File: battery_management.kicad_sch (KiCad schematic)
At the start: 25 parts, among them J3 Conn_01x02, J7 Conn_01x02, Q1 CSD18534Q5A, Q2 CSD18534Q5A, Q3 Si7465DP, U1 BQ25896RTWT, U2 BQ29705DSET

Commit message: footprints
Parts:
- C_BAT1, C_IN1: footprint (none) -> Capacitor_SMD:C_0805_2012Metric
- C_BTST1: renamed from C_BTST; footprint (none) -> Capacitor_SMD:C_0402_1005Metric
- C_PMID1: renamed from C_PMID; footprint (none) -> Capacitor_SMD:C_0402_1005Metric
- C_PROT1: renamed from C_PROT; footprint (none) -> Capacitor_SMD:C_0402_1005Metric
- C_REGN1: renamed from C_REGN; footprint (none) -> Capacitor_SMD:C_0402_1005Metric
- C_SYS1: renamed from C_SYS; footprint (none) -> Capacitor_SMD:C_0805_2012Metric
- J3: footprint (none) -> Connector_Wire:SolderWire-2.5sqmm_1x02_P8.8mm_D2.4mm_OD4.4mm
- J7: footprint (none) -> Connector_Wire:SolderWire-0.5sqmm_1x02_P4.6mm_D0.9mm_OD2.1mm
- L1: footprint (none) -> Inductor_SMD:L_7.3x7.3_H3.5
- R1, R19, R2, R20, R5, R_G1, R_G2: footprint (none) -> Resistor_SMD:R_0402_1005Metric
- R_QON1: renamed from R_QON; footprint (none) -> Resistor_SMD:R_0402_1005Metric
- R_REV1: renamed from R_REV; footprint (none) -> Resistor_SMD:R_0402_1005Metric
- R_SENSE_FG1: renamed from R_SENSE_FG; footprint (none) -> Resistor_SMD:R_2512_6332Metric
- U1: footprint RTW0024H -> Package_DFN_QFN:Texas_RTW_WQFN-24-1EP_4x4mm_P0.5mm_EP2.7x2.7mm_ThermalVias
- U2: footprint DSE0006A -> BQ29705DSET:SON50P150X150X80-6N
- renumbered Q3 to Q_REV1
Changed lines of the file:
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@@
 		(dnp no)
 		(fields_autoplaced yes)
-		(property "Reference" "C_PROT"
+		(property "Reference" "C_PROT1"
 			(at 38.1 123.1899 0)
 			(effects
@@
 			)
 		)
-		(property "Footprint" ""
+		(property "Footprint" "Capacitor_SMD:C_0402_1005Metric"
 			(at 35.2552 128.27 0)
 			(effects
@@
 			(project ""
 				(path "/96bcf3cc-a3b8-4386-8709-07acaf7b6253/a4f15ca0-ce5b-4b53-a9db-308ad3d3fa71"
-					(reference "C_PROT")
+					(reference "C_PROT1")
 					(unit 1)
 				)
@@
 		(dnp no)
 		(fields_autoplaced yes)
-		(property "Reference" "C_SYS"
+		(property "Reference" "C_SYS1"
 			(at 95.25 49.5299 0)
 			(effects
@@
 			)
 		)
-		(property "Footprint" ""
+		(property "Footprint" "Capacitor_SMD:C_0805_2012Metric"
 			(at 92.4052 54.61 0)
 			(effects
@@
 			(project ""
 				(path "/96bcf3cc-a3b8-4386-8709-07acaf7b6253/a4f15ca0-ce5b-4b53-a9db-308ad3d3fa71"
-					(reference "C_SYS")
+					(reference "C_SYS1")
 					(unit 1)
 				)
@@
 		(dnp no)
 		(fields_autoplaced yes)
-		(property "Reference" "R_SENSE_FG"
+		(property "Reference" "R_SENSE_FG1"
 			(at 147.32 143.5099 0)
 			(effects
@@
 			)
 		)
-		(property "Footprint" ""
+		(property "Footprint" "Resistor_SMD:R_2512_6332Metric"
 			(at 143.002 144.78 90)
 			(effects
@@
 			(project ""
 				(path "/96bcf3cc-a3b8-4386-8709-07acaf7b6253/a4f15ca0-ce5b-4b53-a9db-308ad3d3fa71"
-					(reference "R_SENSE_FG")
+					(reference "R_SENSE_FG1")
 					(unit 1)
 				)
@@
 			)
 		)
-		(property "Footprint" ""
+		(property "Footprint" "Capacitor_SMD:C_0805_2012Metric"
 			(at 37.7952 38.1 0)
 			(effects
@@
 		(dnp no)
 		(fields_autoplaced yes)
-		(property "Reference" "R_REV"
+		(property "Reference" "R_REV1"
 			(at 101.6 116.8399 0)
 			(effects
@@
 			)
 		)
-		(property "Footprint" ""
+		(property "Footprint" "Resistor_SMD:R_0402_1005Metric"
 			(at 97.282 118.11 90)
 			(effects
@@
 			(project ""
 				(path "/96bcf3cc-a3b8-4386-8709-07acaf7b6253/a4f15ca0-ce5b-4b53-a9db-308ad3d3fa71"
-					(reference "R_REV")
+					(reference "R_REV1")
 					(unit 1)
 				)
@@
 		(dnp no)
 		(fields_autoplaced yes)
-		(property "Reference" "C_REGN"
+		(property "Reference" "C_REGN1"
 			(at 93.98 62.2299 0)
 			(effects
@@
 			)
 		)
-		(property "Footprint" ""
+		(property "Footprint" "Capacitor_SMD:C_0402_1005Metric"
 			(at 91.1352 67.31 0)
 			(effects
@@
 			(project ""
 				(path "/96bcf3cc-a3b8-4386-8709-07acaf7b6253/a4f15ca0-ce5b-4b53-a9db-308ad3d3fa71"
-					(reference "C_REGN")
+					(reference "C_REGN1")
 					(unit 1)
 				)
@@
 		(dnp no)
 		(fields_autoplaced yes)
-		(property "Reference" "R_QON"
+		(property "Reference" "R_QON1"
 			(at 101.6 80.0099 0)
 			(effects
@@
 			)
 		)
-		(property "Footprint" ""
+		(property "Footprint" "Resistor_SMD:R_0402_1005Metric"
 			(at 97.282 81.28 90)
 			(effects
@@
 			(project ""
 				(path "/96bcf3cc-a3b8-4386-8709-07acaf7b6253/a4f15ca0-ce5b-4b53-a9db-308ad3d3fa71"
-					(reference "R_QON")
+					(reference "R_QON1")
 					(unit 1)
 				)
@@
 			)
 		)
-		(property "Footprint" ""
+		(property "Footprint" "Resistor_SMD:R_0402_1005Metric"
 			(at 87.122 86.36 90)
 			(effects
@@
 			)
 		)
-		(property "Footprint" ""
+		(property "Footprint" "Resistor_SMD:R_0402_1005Metric"
 			(at 61.722 114.3 90)
 			(effects
@@
 			)
 		)
-		(property "Footprint" ""
+		(property "Footprint" "Inductor_SMD:L_7.3x7.3_H3.5"
 			(at 104.14 45.72 0)
 			(effects
@@
 		(dnp no)
 		(fields_autoplaced yes)
-		(property "Reference" "C_PMID"
+		(property "Reference" "C_PMID1"
 			(at 41.91 44.4499 0)
 			(effects
@@
 			)
 		)
-		(property "Footprint" ""
+		(property "Footprint" "Capacitor_SMD:C_0402_1005Metric"
 			(at 39.0652 49.53 0)
 			(effects
@@
 			(project ""
 				(path "/96bcf3cc-a3b8-4386-8709-07acaf7b6253/a4f15ca0-ce5b-4b53-a9db-308ad3d3fa71"
-					(reference "C_PMID")
+					(reference "C_PMID1")
 					(unit 1)
 				)
@@
 			)
 		)
-		(property "Footprint" ""
+		(property "Footprint" "Resistor_SMD:R_0402_1005Metric"
 			(at 101.092 93.98 90)
 			(effects
@@
 			)
 		)
-		(property "Footprint" ""
+		(property "Footprint" "Resistor_SMD:R_0402_1005Metric"
 			(at 82.042 148.59 90)
 			(effects
@@
 		(dnp no)
 		(fields_autoplaced yes)
-		(property "Reference" "C_BTST"
+		(property "Reference" "C_BTST1"
 			(at 93.98 36.8299 0)
 			(effects
@@
 			)
 		)
-		(property "Footprint" ""
+		(property "Footprint" "Capacitor_SMD:C_0402_1005Metric"
 			(at 91.1352 41.91 0)
 			(effects
@@
 			(project ""
 				(path "/96bcf3cc-a3b8-4386-8709-07acaf7b6253/a4f15ca0-ce5b-4b53-a9db-308ad3d3fa71"
-					(reference "C_BTST")
+					(reference "C_BTST1")
 					(unit 1)
 				)
@@
 			)
 		)
-		(property "Footprint" "DSE0006A"
+		(property "Footprint" "BQ29705DSET:SON50P150X150X80-6N"
 			(at 63.5 139.7 0)
 			(effects
@@
 			)
 		)
-		(property "Footprint" "RTW0024H"
+		(property "Footprint" "Package_DFN_QFN:Texas_RTW_WQFN-24-1EP_4x4mm_P0.5mm_EP2.7x2.7mm_ThermalVias"
 			(at 63.5 68.58 0)
 			(effects
@@
 			)
 		)
-		(property "Footprint" ""
+		(property "Footprint" "Connector_Wire:SolderWire-0.5sqmm_1x02_P4.6mm_D0.9mm_OD2.1mm"
 			(at 128.27 90.17 0)
 			(effects
@@
 			)
 		)
-		(property "Footprint" ""
+		(property "Footprint" "Resistor_SMD:R_0402_1005Metric"
 			(at 84.582 135.89 90)
 			(effects
@@
 			)
 		)
-		(property "Footprint" ""
+		(property "Footprint" "Resistor_SMD:R_0402_1005Metric"
 			(at 31.242 53.34 90)
 			(effects
@@
 			)
 		)
-		(property "Footprint" ""
+		(property "Footprint" "Capacitor_SMD:C_0805_2012Metric"
 			(at 103.8352 73.66 0)
 			(effects
@@
 			)
 		)
-		(property "Footprint" ""
+		(property "Footprint" "Connector_Wire:SolderWire-2.5sqmm_1x02_P8.8mm_D2.4mm_OD4.4mm"
 			(at 161.29 119.38 0)
 			(effects
@@
 			)
 		)
-		(property "Footprint" ""
+		(property "Footprint" "Resistor_SMD:R_0402_1005Metric"
 			(at 94.742 147.32 90)
 			(effects
@@
 		(dnp no)
 		(fields_autoplaced yes)
-		(property "Reference" "Q3"
+		(property "Reference" "Q_REV1"
 			(at 118.11 113.0299 0)
 			(effects
@@
 			(project ""
 				(path "/96bcf3cc-a3b8-4386-8709-07acaf7b6253/a4f15ca0-ce5b-4b53-a9db-308ad3d3fa71"
-					(reference "Q3")
-					(unit 1)
-				)
+					(reference "Q_REV1")
+					(unit 1)
+				)

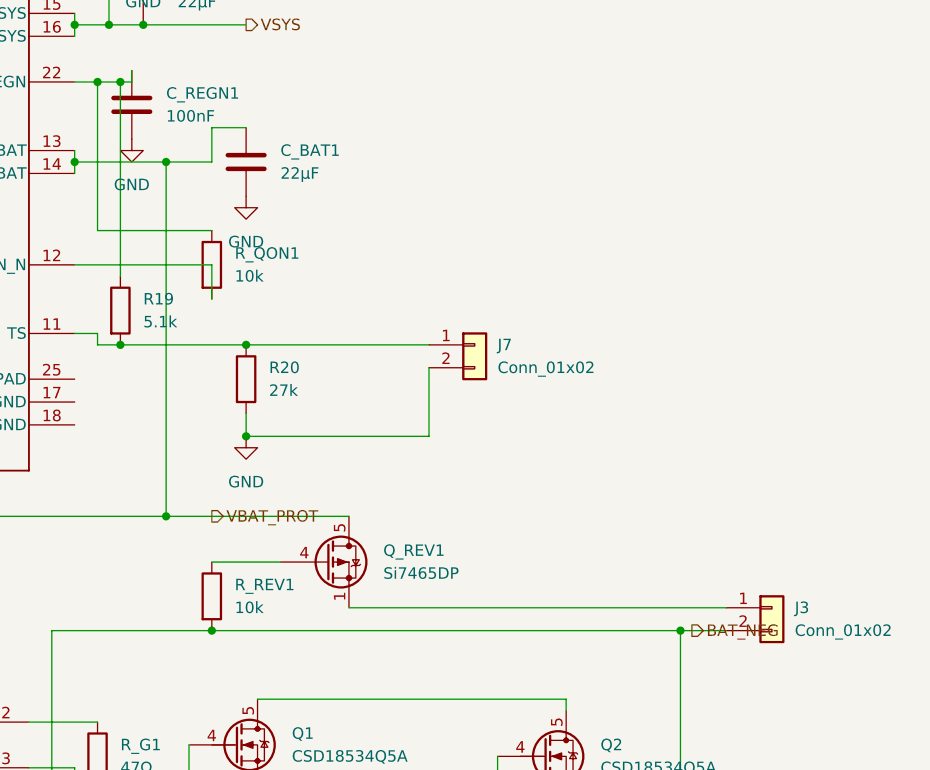
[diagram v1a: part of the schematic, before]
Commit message: fix missing connections, complete footprints
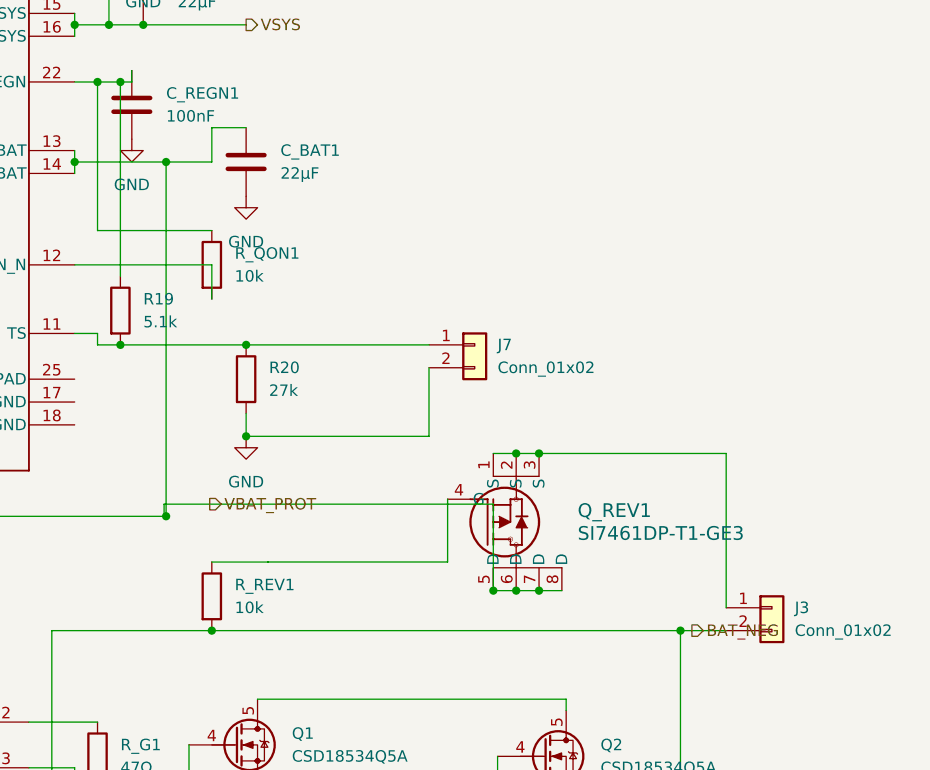
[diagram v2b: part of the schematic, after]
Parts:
- removed Q_REV1: Si7465DP, Package_SO:PowerPAK_SO-8_Single, symbol Si7461DP:Si7465DP
- added Q_REV1: SI7461DP-T1-GE3, Package_SO:PowerPAK_SO-8_Single, symbol Si7461DP-T1-GE3:SI7461DP-T1-GE3
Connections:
- net VBAT_PROT: now also Q_REV1.5 (D), Q_REV1.6 (D), Q_REV1.7 (D), Q_REV1.8 (D)
- net at R_REV1.1: now also Q_REV1.4 (G)
- net at J3.1 (Pin_1): now also Q_REV1.1 (S), Q_REV1.2 (S), Q_REV1.3 (S)
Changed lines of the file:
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@@
 	)
 	(junction
+		(at 130.3354 117.4769)
+		(diameter 0)
+		(color 0 0 0 0)
+	)
+	(junction
 		(at 83.82 54.61)
 		(diameter 0)
@@
 	)
 	(junction
+		(at 132.8754 102.2369)
+		(diameter 0)
+		(color 0 0 0 0)
+	)
+	(junction
 		(at 151.13 121.92)
 		(diameter 0)
@@
 	)
 	(junction
-		(at 99.06 121.92)
+		(at 135.4154 102.2369)
 		(diameter 0)
 		(color 0 0 0 0)
 	)
 	(junction
-		(at 91.44 54.61)
+		(at 132.8754 117.4769)
 		(diameter 0)
 		(color 0 0 0 0)
 	)
 	(junction
-		(at 88.9 60.96)
+		(at 93.98 109.2118)
 		(diameter 0)
 		(color 0 0 0 0)
 	)
 	(junction
-		(at 93.98 109.22)
+		(at 135.4154 117.4769)
+		(diameter 0)
+		(color 0 0 0 0)
+	)
+	(junction
+		(at 99.06 121.92)
+		(diameter 0)
+		(color 0 0 0 0)
+	)
+	(junction
+		(at 91.44 54.61)
+		(diameter 0)
+		(color 0 0 0 0)
+	)
+	(junction
+		(at 88.9 60.96)
 		(diameter 0)
 		(color 0 0 0 0)
@@
 	(wire
 		(pts
-			(xy 156.21 119.38) (xy 114.3 119.38)
+			(xy 93.7521 107.8693) (xy 93.7521 109.2118)
+		)
+		(stroke
+			(width 0)
+			(type default)
+		)
+	)
+	(wire
+		(pts
+			(xy 132.8754 102.2369) (xy 135.4154 102.2369)
 		)
 		(stroke
@@
 	(wire
 		(pts
-			(xy 99.06 114.3) (xy 106.68 114.3)
+			(xy 105.2984 114.2918) (xy 125.2554 114.2918)
 		)
 		(stroke
@@
 	(wire
 		(pts
+			(xy 130.3354 107.8693) (xy 130.3354 117.4769)
+		)
+		(stroke
+			(width 0)
+			(type default)
+		)
+	)
+	(wire
+		(pts
 			(xy 96.52 151.13) (xy 104.14 151.13)
 		)
@@
 	(wire
 		(pts
+			(xy 93.98 109.2118) (xy 93.98 109.22)
+		)
+		(stroke
+			(width 0)
+			(type default)
+		)
+	)
+	(wire
+		(pts
 			(xy 78.74 132.08) (xy 86.36 132.08)
 		)
@@
 	(wire
 		(pts
+			(xy 105.2984 114.2918) (xy 105.2984 114.3)
+		)
+		(stroke
+			(width 0)
+			(type default)
+		)
+	)
+	(wire
+		(pts
 			(xy 99.06 69.85) (xy 99.06 66.04)
 		)
@@
 	(wire
 		(pts
-			(xy 93.98 109.22) (xy 114.3 109.22)
+			(xy 93.7521 107.8693) (xy 130.3354 107.8693)
 		)
 		(stroke
@@
 	(wire
 		(pts
+			(xy 135.4154 102.2369) (xy 156.21 102.2369)
+		)
+		(stroke
+			(width 0)
+			(type default)
+		)
+	)
+	(wire
+		(pts
 			(xy 78.74 137.16) (xy 83.82 137.16)
 		)
@@
 	(wire
 		(pts
+			(xy 132.8754 117.4769) (xy 135.4154 117.4769)
+		)
+		(stroke
+			(width 0)
+			(type default)
+		)
+	)
+	(wire
+		(pts
 			(xy 83.82 45.72) (xy 83.82 46.99)
 		)
@@
 	(wire
 		(pts
+			(xy 135.4154 117.4769) (xy 137.9554 117.4769)
+		)
+		(stroke
+			(width 0)
+			(type default)
+		)
+	)
+	(wire
+		(pts
 			(xy 48.26 124.46) (xy 48.26 132.08)
 		)
@@
 	(wire
 		(pts
+			(xy 125.2554 114.2918) (xy 125.2554 107.3169)
+		)
+		(stroke
+			(width 0)
+			(type default)
+		)
+	)
+	(wire
+		(pts
 			(xy 104.14 144.78) (xy 109.22 144.78)
 		)
@@
 	(wire
 		(pts
-			(xy 93.98 69.85) (xy 93.98 109.22)
+			(xy 93.98 69.85) (xy 93.98 109.2118)
+		)
+		(stroke
+			(width 0)
+			(type default)
+		)
+	)
+	(wire
+		(pts
+			(xy 156.21 102.2369) (xy 156.21 119.38)
 		)
 		(stroke
@@
 	(wire
 		(pts
+			(xy 130.3354 102.2369) (xy 132.8754 102.2369)
+		)
+		(stroke
+			(width 0)
+			(type default)
+		)
+	)
+	(wire
+		(pts
 			(xy 33.02 53.34) (xy 43.18 53.34)
 		)
@@
 	(wire
 		(pts
+			(xy 105.2984 114.3) (xy 99.06 114.3)
+		)
+		(stroke
+			(width 0)
+			(type default)
+		)
+	)
+	(wire
+		(pts
 			(xy 90.17 44.45) (xy 104.14 44.45)
 		)
@@
 	(wire
 		(pts
+			(xy 130.3354 117.4769) (xy 132.8754 117.4769)
+		)
+		(stroke
+			(width 0)
+			(type default)
+		)
+	)
+	(wire
+		(pts
+			(xy 93.7521 109.2118) (xy 93.98 109.2118)
+		)
+		(stroke
+			(width 0)
+			(type default)
+		)
+	)
+	(wire
+		(pts
 			(xy 83.82 152.4) (xy 130.81 152.4)
 		)
@@
 	(hierarchical_label "VBAT_PROT"
 		(shape output)
-		(at 99.06 109.22 0)
+		(at 98.8321 107.8693 0)
 		(effects
 			(font
@@
 	)
 	(symbol
+		(lib_id "Si7461DP-T1-GE3:SI7461DP-T1-GE3")
+		(at 125.2554 107.3169 0)
+		(unit 1)
+		(exclude_from_sim no)
+		(in_bom yes)
+		(on_board yes)
+		(dnp no)
+		(fields_autoplaced yes)
+		(property "Reference" "Q_REV1"
+			(at 139.7 108.5868 0)
+			(effects
+				(font
+					(size 1.524 1.524)
+				)
+				(justify left)
+			)
+		)
+		(property "Value" "SI7461DP-T1-GE3"
+			(at 139.7 111.1268 0)
+			(effects
+				(font
+					(size 1.524 1.524)
+				)
+				(justify left)
+			)
+		)
+		(property "Footprint" "Package_SO:PowerPAK_SO-8_Single"
+			(at 125.2554 107.3169 0)
+			(effects
+				(font
+					(size 1.27 1.27)
+					(italic yes)
+				)
+				(hide yes)
+			)
+		)
+		(property "Datasheet" "https://www.vishay.com/doc?72567"
+			(at 125.2554 107.3169 0)
+			(effects
+				(font
+					(size 1.27 1.27)
+					(italic yes)
+				)
+				(hide yes)
+			)
+		)
+		(property "Description" ""
+			(at 125.2554 107.3169 0)
+			(effects
+				(font
+					(size 1.27 1.27)
+				)
+				(hide yes)
+			)
+		)
+		(pin "6"
+		)
+		(pin "3"
+		)
+		(pin "2"
+		)
+		(pin "5"
+		)
+		(pin "1"
+		)
+		(pin "8"
+		)
+		(pin "7"
+		)
+		(pin "4"
+		)
+		(instances
+			(project ""
+				(path "/96bcf3cc-a3b8-4386-8709-07acaf7b6253/a4f15ca0-ce5b-4b53-a9db-308ad3d3fa71"
+					(reference "Q_REV1")
+					(unit 1)
+				)
+			)
+		)
+	)
+	(symbol
 		(lib_id "Device:R")
 		(at 86.36 135.89 0)
@@
 					(unit 1)
 				)
-			)
-		)
-	)
-	(symbol
-		(lib_id "Si7461DP:Si7465DP")
-		(at 111.76 114.3 0)
-		(unit 1)
-		(exclude_from_sim no)
-		(in_bom yes)
-		(on_board yes)
-		(dnp no)
-		(fields_autoplaced yes)
-		(property "Reference" "Q_REV1"
-			(at 118.11 113.0299 0)
-			(effects
-				(font
-					(size 1.27 1.27)
-				)
-				(justify left)
-			)
-		)
-		(property "Value" "Si7465DP"
-			(at 118.11 115.5699 0)
-			(effects
-				(font
-					(size 1.27 1.27)
-				)
-				(justify left)
-			)
-		)
-		(property "Footprint" "Package_SO:PowerPAK_SO-8_Single"
-			(at 116.84 116.205 0)
-			(effects
-				(font
-					(size 1.27 1.27)
-					(italic yes)
-				)
-				(justify left)
-				(hide yes)
-			)
-		)
-		(property "Datasheet" ""
-			(at 111.76 114.3 0)
-			(effects
-				(font
-					(size 1.27 1.27)
-				)
-				(justify left)
-				(hide yes)
-			)
-		)
-		(property "Description" ""
-			(at 111.76 114.3 0)
-			(effects
-				(font
-					(size 1.27 1.27)
-				)
-				(hide yes)
-			)
-		)
-		(pin "8"
-		)
-		(pin "5"
-		)
-		(pin "1"
-		)
-		(pin "4"
-		)
-		(pin "3"
-		)
-		(pin "2"
-		)
-		(pin "7"
-		)
-		(pin "6"
-		)
-		(instances
-			(project ""
-				(path "/96bcf3cc-a3b8-4386-8709-07acaf7b6253/a4f15ca0-ce5b-4b53-a9db-308ad3d3fa71"
-					(reference "Q_REV1")
-					(unit 1)
-				)

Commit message: net labels
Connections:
- net PROT_BAT: now reaches C_PROT1.1, R1.2, U2.5 (BAT)
- net QREV_GATE: now reaches Q_REV1.4 (G), R_REV1.1
- net CHG_REGN: now reaches C_REGN1.1, R19.1, R_QON1.1, U1.22 (REGN)
- net CHG_QON: now reaches R_QON1.2, U1.12 (QON_N)
- net NTC_TS: now reaches J7.1 (Pin_1), R19.2, R20.1, U1.11 (TS)
- net Q2_GATE: now reaches Q2.4 (G), R_G2.2
- net PROT_MID: now reaches Q1.5 (D), Q2.5 (D)
- net CHG_SW: now reaches C_BTST1.2, L1.1, U1.19 (SW), U1.20 (SW)
- net PMID: now reaches C_PMID1.1, U1.23 (PMID)
- net PROT_DOUT: now reaches R_G2.1, U2.3 (DOUT)
- net CHG_BTST: now reaches C_BTST1.1, U1.21 (BTST)
- net PROT_COUT: now reaches R_G1.1, U2.2 (COUT)
- net PROT_V-: now reaches R2.1, U2.6 (V-)
- net Q1_GATE: now reaches Q1.4 (G), R_G1.2
- net CHG_ILIM: now reaches R5.1, U1.10 (ILIM)
- net VBAT_RAW: now reaches J3.1 (Pin_1), Q_REV1.1 (S), Q_REV1.2 (S), Q_REV1.3 (S)
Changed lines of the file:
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@@
+		)
+	)
+	(label "NTC_TS"
+		(at 115.5591 90.17 0)
+		(effects
+			(font
+				(size 1.27 1.27)
+			)
+			(justify left bottom)
+		)
+	)
+	(label "Q1_GATE"
+		(at 96.52 137.5556 0)
+		(effects
+			(font
+				(size 1.27 1.27)
+			)
+			(justify left bottom)
+		)
+	)
+	(label "VBAT_RAW"
+		(at 156.21 115.824 0)
+		(effects
+			(font
+				(size 1.27 1.27)
+			)
+			(justify left bottom)
+		)
+	)
+	(label "PROT_BAT"
+		(at 48.26 126.9171 0)
+		(effects
+			(font
+				(size 1.27 1.27)
+			)
+			(justify left bottom)
+		)
+	)
+	(label "QREV_GATE"
+		(at 125.2554 110.8436 0)
+		(effects
+			(font
+				(size 1.27 1.27)
+			)
+			(justify left bottom)
+		)
+	)
+	(label "PROT_DOUT"
+		(at 82.7912 137.16 0)
+		(effects
+			(font
+				(size 1.27 1.27)
+			)
+			(justify left bottom)
+		)
+	)
+	(label "PROT_V-"
+		(at 87.9166 142.24 0)
+		(effects
+			(font
+				(size 1.27 1.27)
+			)
+			(justify left bottom)
+		)
+	)
+	(label "PROT_MID"
+		(at 106.8874 129.54 0)
+		(effects
+			(font
+				(size 1.27 1.27)
+			)
+			(justify left bottom)
+		)
+	)
+	(label "PROT_COUT"
+		(at 82.8827 132.08 0)
+		(effects
+			(font
+				(size 1.27 1.27)
+			)
+			(justify left bottom)
+		)
+	)
+	(label "CHG_REGN"
+		(at 84.8064 60.96 0)
+		(effects
+			(font
+				(size 1.27 1.27)
+			)
+			(justify left bottom)
+		)
+	)
+	(label "CHG_SW"
+		(at 90.17 42.9563 0)
+		(effects
+			(font
+				(size 1.27 1.27)
+			)
+			(justify left bottom)
+		)
+	)
+	(label "CHG_QON"
+		(at 84.8613 81.28 0)
+		(effects
+			(font
+				(size 1.27 1.27)
+			)
+			(justify left bottom)
+		)
+	)
+	(label "CHG_ILIM"
+		(at 41.3931 53.34 0)
+		(effects
+			(font
+				(size 1.27 1.27)
+			)
+			(justify left bottom)
+		)
+	)
+	(label "PMID"
+		(at 41.0165 45.72 0)
+		(effects
+			(font
+				(size 1.27 1.27)
+			)
+			(justify left bottom)
+		)
+	)
+	(label "CHG_BTST"
+		(at 85.5022 38.1 0)
+		(effects
+			(font
+				(size 1.27 1.27)
+			)
+			(justify left bottom)
+		)
+	)
+	(label "Q2_GATE"
+		(at 130.81 143.0906 0)
+		(effects
+			(font
+				(size 1.27 1.27)
+			)
+			(justify left bottom)
 		)
 	)
